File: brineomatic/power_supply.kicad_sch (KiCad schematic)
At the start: 31 parts, among them J10 5.08MM, J9 5.08MM, Q3 20N06, U2 LM74700, U3 XL1509-5.0, U4 MAX40200AUK

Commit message: small cleanups on schematic
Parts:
- D17: value RED -> GREEN; LCSC C965799 -> (none)
- R20: value 10k -> 5.1k
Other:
- moved on the sheet: C10, C11, C12, C13, C6, C8, D18, D19, D20, F2, FB1, L1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

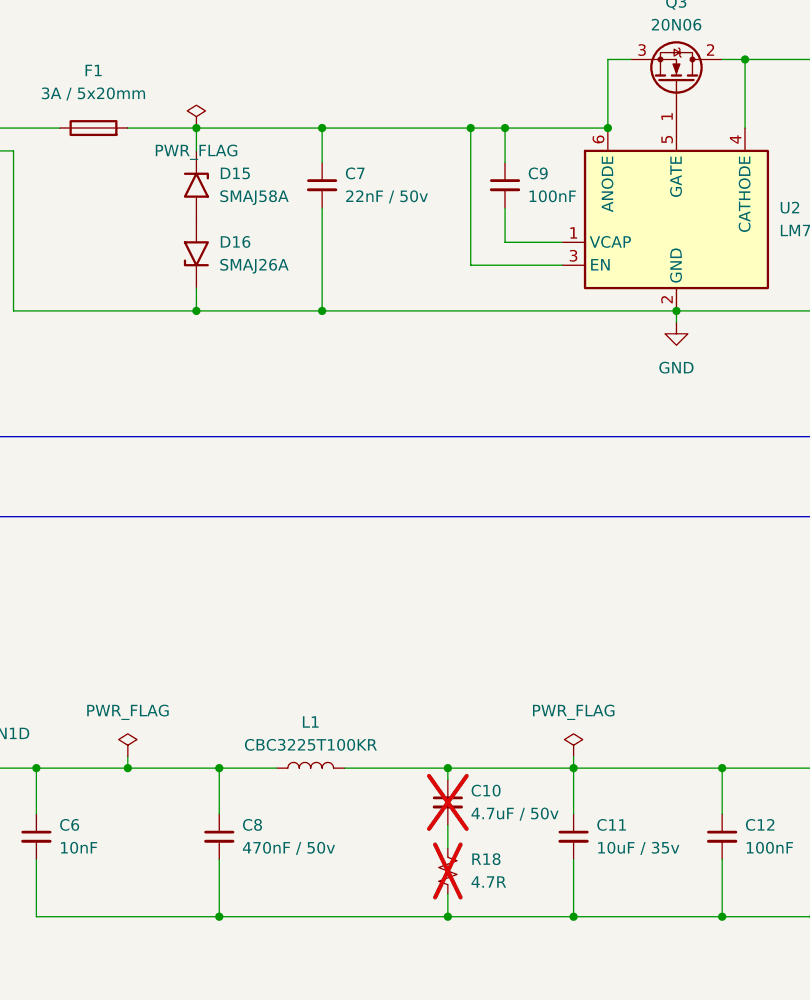
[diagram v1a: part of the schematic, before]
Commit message: added back up usb serial converter headers
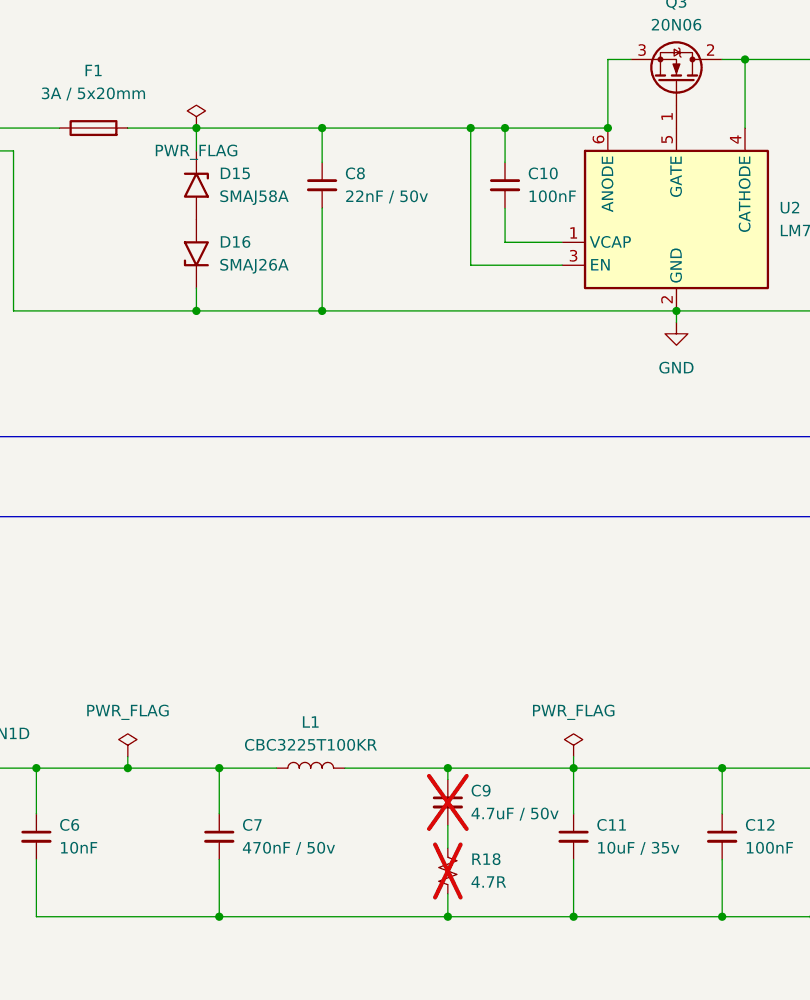
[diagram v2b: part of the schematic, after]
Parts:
- renumbered C9 to C10, C8 to C7, C7 to C8, C10 to C9
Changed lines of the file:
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@@
 		(dnp no)
 		(fields_autoplaced yes)
-		(property "Reference" "#FLG02"
+		(property "Reference" "#FLG01"
 			(at 68.58 120.015 0)
 			(effects
@@
 			(project "brineomatic"
 				(path "/96477ae2-ef08-48f3-8dd4-fe4478541f68/7cbb3b3c-cf93-4880-b816-c6df902b993c"
-					(reference "#FLG02")
+					(reference "#FLG01")
 					(unit 1)
 				)
@@
 		(on_board yes)
 		(dnp no)
-		(property "Reference" "C7"
+		(property "Reference" "C8"
 			(at 92.71 57.1563 0)
 			(effects
@@
 			(project "brineomatic"
 				(path "/96477ae2-ef08-48f3-8dd4-fe4478541f68/7cbb3b3c-cf93-4880-b816-c6df902b993c"
-					(reference "C7")
+					(reference "C8")
 					(unit 1)
 				)
@@
 		(dnp no)
 		(fields_autoplaced yes)
-		(property "Reference" "C9"
+		(property "Reference" "C10"
 			(at 113.03 57.1563 0)
 			(effects
@@
 			(project "brineomatic"
 				(path "/96477ae2-ef08-48f3-8dd4-fe4478541f68/7cbb3b3c-cf93-4880-b816-c6df902b993c"
-					(reference "C9")
+					(reference "C10")
 					(unit 1)
 				)
@@
 		(dnp yes)
 		(fields_autoplaced yes)
-		(property "Reference" "C10"
+		(property "Reference" "C9"
 			(at 106.68 125.7363 0)
 			(effects
@@
 			(project "brineomatic"
 				(path "/96477ae2-ef08-48f3-8dd4-fe4478541f68/7cbb3b3c-cf93-4880-b816-c6df902b993c"
-					(reference "C10")
+					(reference "C9")
 					(unit 1)
 				)
@@
 		(on_board yes)
 		(dnp no)
-		(property "Reference" "#FLG01"
+		(property "Reference" "#FLG02"
 			(at 76.2 50.165 0)
 			(effects
@@
 			(project "brineomatic"
 				(path "/96477ae2-ef08-48f3-8dd4-fe4478541f68/7cbb3b3c-cf93-4880-b816-c6df902b993c"
-					(reference "#FLG01")
+					(reference "#FLG02")
 					(unit 1)
 				)
@@
 		(dnp no)
 		(fields_autoplaced yes)
-		(property "Reference" "C8"
+		(property "Reference" "C7"
 			(at 81.28 129.5463 0)
 			(effects
@@
 			(project "brineomatic"
 				(path "/96477ae2-ef08-48f3-8dd4-fe4478541f68/7cbb3b3c-cf93-4880-b816-c6df902b993c"
-					(reference "C8")
+					(reference "C7")
 					(unit 1)
 				)

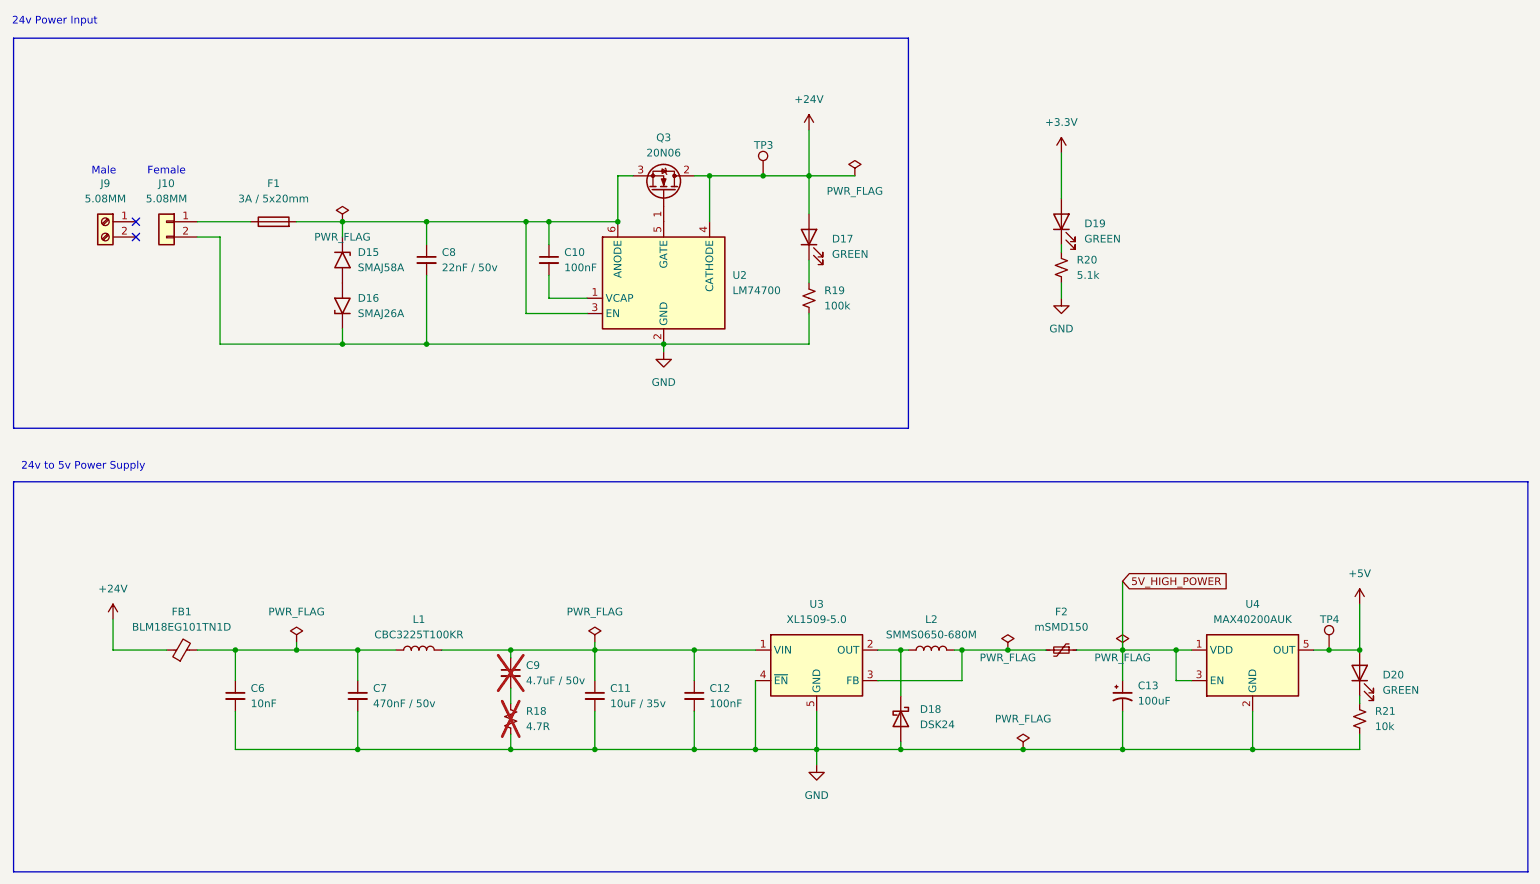
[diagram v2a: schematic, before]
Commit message: added missing gnd test point
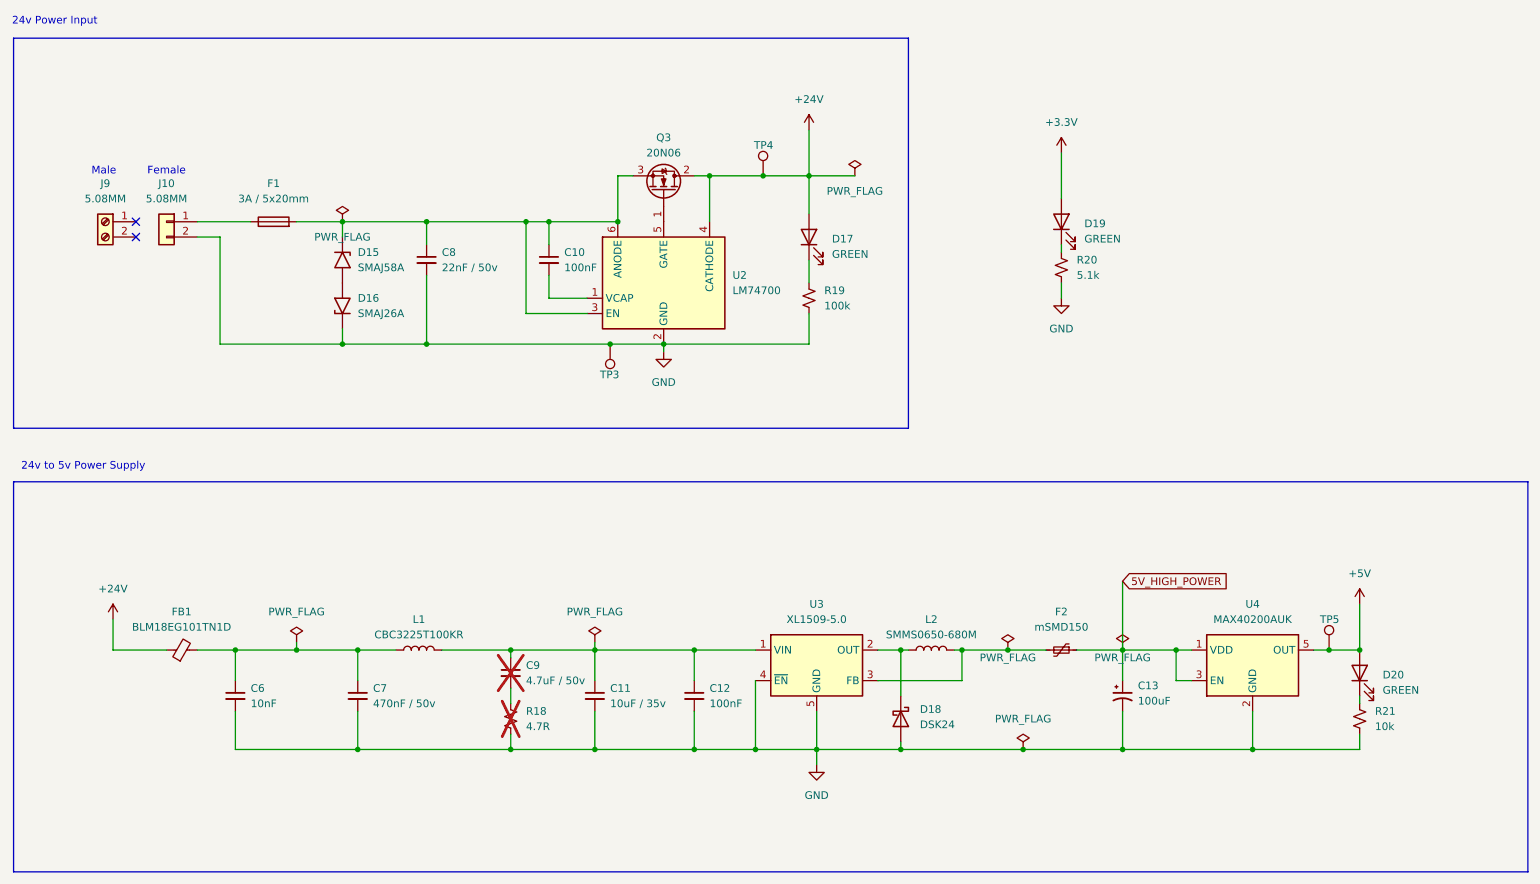
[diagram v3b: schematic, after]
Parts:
- added TP3: ~, TestPoint:TestPoint_THTPad_D1.5mm_Drill0.7mm, symbol Connector:TestPoint
- renumbered TP3 to TP4, TP4 to TP5
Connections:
- net GND: now also TP3.1
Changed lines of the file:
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@@
 		(color 0 0 0 0)
 	)
+	(junction
+		(at 120.65 72.39)
+		(diameter 0)
+		(color 0 0 0 0)
+	)
 	(no_connect
 		(at 41.91 52.07)
@@
 	(wire
 		(pts
-			(xy 90.17 72.39) (xy 129.54 72.39)
+			(xy 90.17 72.39) (xy 120.65 72.39)
 		)
 		(stroke
@@
 	(wire
 		(pts
+			(xy 120.65 72.39) (xy 129.54 72.39)
+		)
+		(stroke
+			(width 0)
+			(type default)
+		)
+	)
+	(wire
+		(pts
 			(xy 118.11 133.35) (xy 118.11 139.7)
 		)
@@
 		(on_board yes)
 		(dnp no)
-		(property "Reference" "TP3"
+		(property "Reference" "TP4"
 			(at 144.526 39.37 0)
 			(effects
@@
 			(project "brineomatic"
 				(path "/96477ae2-ef08-48f3-8dd4-fe4478541f68/7cbb3b3c-cf93-4880-b816-c6df902b993c"
-					(reference "TP3")
+					(reference "TP4")
 					(unit 1)
 				)
@@
 		(on_board yes)
 		(dnp no)
-		(property "Reference" "TP4"
+		(property "Reference" "TP5"
 			(at 238.506 118.11 0)
 			(effects
@@
 			(project "brineomatic"
 				(path "/96477ae2-ef08-48f3-8dd4-fe4478541f68/7cbb3b3c-cf93-4880-b816-c6df902b993c"
-					(reference "TP4")
+					(reference "TP5")
 					(unit 1)
 				)
@@
 					(unit 1)
 				)
+			)
+		)
+	)
+	(symbol
+		(lib_id "Connector:TestPoint")
+		(at 120.65 72.39 180)
+		(unit 1)
+		(exclude_from_sim no)
+		(in_bom no)
+		(on_board yes)
+		(dnp no)
+		(property "Reference" "TP3"
+			(at 122.174 77.47 0)
+			(effects
+				(font
+					(size 1.27 1.27)
+				)
+				(justify left)
+			)
+		)
+		(property "Value" "~"
+			(at 118.11 74.4221 0)
+			(effects
+				(font
+					(size 1.27 1.27)
+				)
+				(justify left)
+				(hide yes)
+			)
+		)
+		(property "Footprint" "TestPoint:TestPoint_THTPad_D1.5mm_Drill0.7mm"
+			(at 115.57 72.39 0)
+			(effects
+				(font
+					(size 1.27 1.27)
+				)
+				(hide yes)
+			)
+		)
+		(property "Datasheet" "~"
+			(at 115.57 72.39 0)
+			(effects
+				(font
+					(size 1.27 1.27)
+				)
+				(hide yes)
+			)
+		)
+		(property "Description" "test point"
+			(at 120.65 72.39 0)
+			(effects
+				(font
+					(size 1.27 1.27)
+				)
+				(hide yes)
+			)
+		)
+		(property "LCSC Part Name" ""
+			(at 120.65 72.39 0)
+			(effects
+				(font
+					(size 1.27 1.27)
+				)
+				(hide yes)
+			)
+		)
+		(property "Manufacturer" ""
+			(at 120.65 72.39 0)
+			(effects
+				(font
+					(size 1.27 1.27)
+				)
+				(hide yes)
+			)
+		)
+		(property "Manufacturer Part" ""
+			(at 120.65 72.39 0)
+			(effects
+				(font
+					(size 1.27 1.27)
+				)
+				(hide yes)
+			)
+		)
+		(property "Supplier" ""
+			(at 120.65 72.39 0)
+			(effects
+				(font
+					(size 1.27 1.27)
+				)
+				(hide yes)
+			)
+		)
+		(property "Supplier Part" ""
+			(at 120.65 72.39 0)
+			(effects
+				(font
+					(size 1.27 1.27)
+				)
+				(hide yes)
+			)
+		)
+		(pin "1"
+		)
+		(instances
+			(project "brineomatic"
+				(path "/96477ae2-ef08-48f3-8dd4-fe4478541f68/7cbb3b3c-cf93-4880-b816-c6df902b993c"
+					(reference "TP3")
+					(unit 1)
+				)

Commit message: added more esd protection to the power rails (24v, 5v, 3.3v)
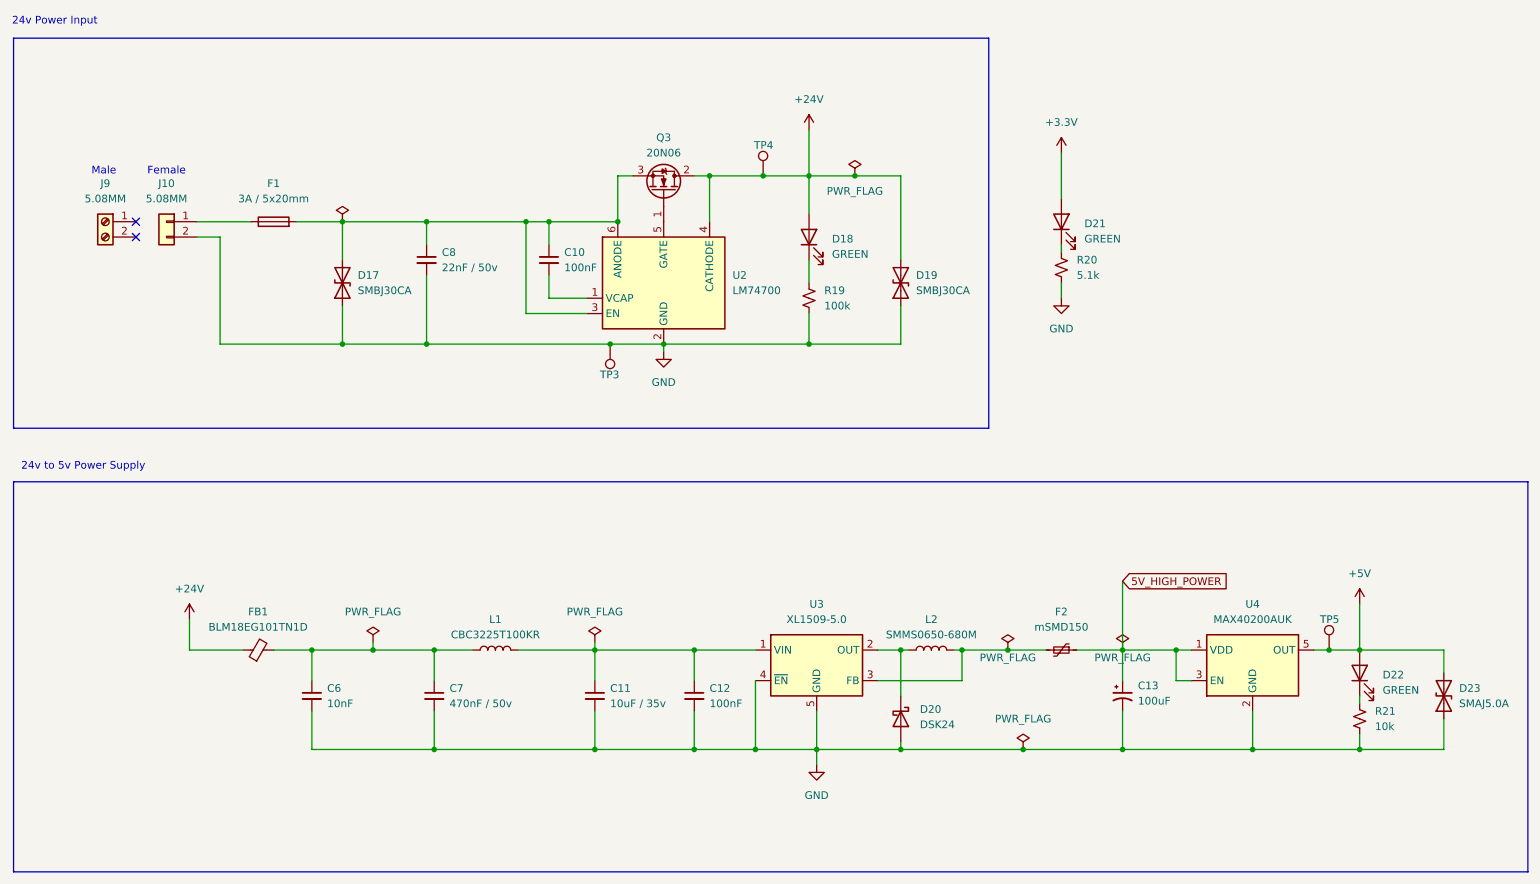
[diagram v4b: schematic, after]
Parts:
- removed C9: 4.7uF / 50v, Capacitor_SMD:C_0603_1608Metric, symbol Device:C_Small
- removed D15: SMAJ58A, Diode_SMD:D_SMA, symbol Diode:SMAJ58A
- removed D16: SMAJ26A, Diode_SMD:D_SMA, symbol Diode:SMAJ26A
- removed R18: 4.7R, Resistor_SMD:R_0603_1608Metric, symbol Device:R_Small_US
- added D17, D19: SMBJ30CA, Diode_SMD:D_SMB, symbol Device:D_TVS
- added D23: SMAJ5.0A, Diode_SMD:D_SMA, symbol Device:D_TVS
- D21: renamed from D19; LCSC C965799 -> (none)
- D22: renamed from D20; LCSC C965799 -> (none)
- renumbered D17 to D18, D18 to D20
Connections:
- net +24V: now also D19.2 (A2)
- net +5V: now also D23.2 (A2)
- net GND: now also D17.1 (A1), D19.1 (A1), D23.1 (A1)
- net at C10.1, C8.1, F1.2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: now also D17.2 (A2)
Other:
- moved on the sheet: C6, C7, FB1, L1
